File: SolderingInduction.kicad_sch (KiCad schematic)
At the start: 56 parts, among them J1 MC-307, J3 RBP_GPIO_CONN, SW1 SW_Push, SW2 SW_Push, SW3 SW_Push, SW4 SW_Push, SW5 SW_Push, SW6 SW_Push, SW7 SW_Push, SW8 SW_Push, U1 SPX2920M3-3.3_SOT223, U2 CAT24C256, U3 W25Q32JVZP, U4 RP2040, Y1 X322512MMB4SI

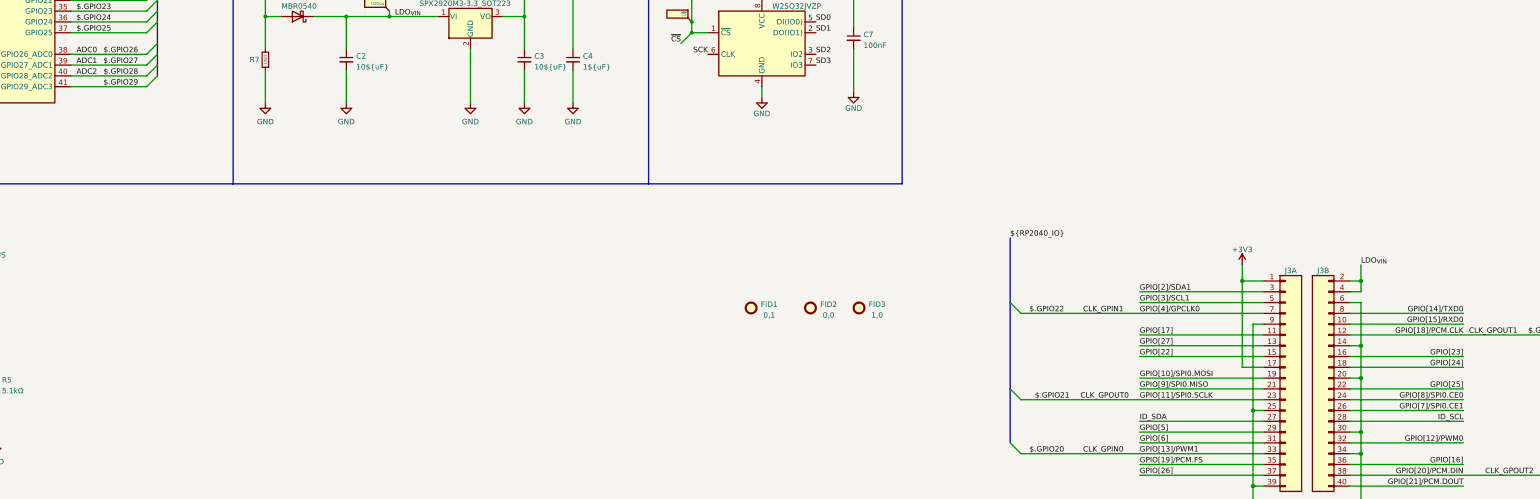
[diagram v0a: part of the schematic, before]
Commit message: Rough layout run to pinheader
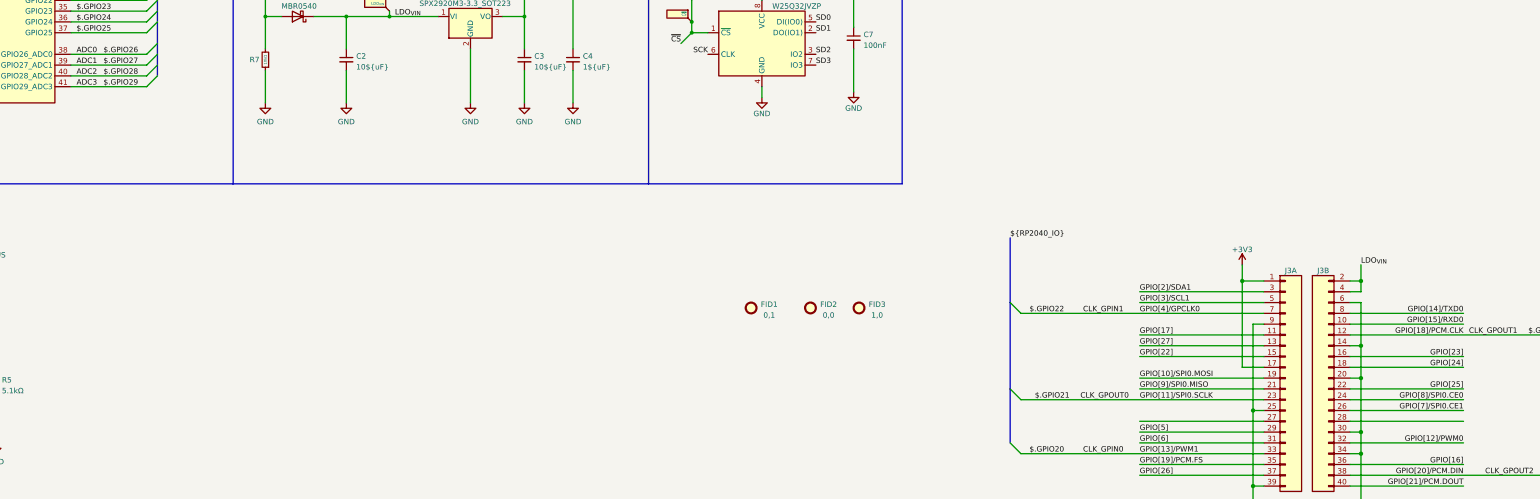
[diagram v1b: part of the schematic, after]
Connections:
- net ID_SCL: no longer J3.28 (Pin_28)
- net ID_SDA: no longer J3.27 (Pin_27)
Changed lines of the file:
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@@
     (effects (font (size 1.27 1.27)) (justify right bottom))
   )
-  (label "BUTTON_DOWN" (at 519.43 49.53 0)
+  (label "ADC3" (at 99.06 104.14 0)
     (effects (font (size 1.27 1.27)) (justify left bottom))
   )
-  (label "ID_SDA" (at 349.25 182.88 0)
+  (label "BUTTON_DOWN" (at 519.43 49.53 0)
     (effects (font (size 1.27 1.27)) (justify left bottom))
   )
@@
     (effects (font (size 1.27 1.27)) (justify left bottom))
   )
-  (label "ID_SCL" (at 425.45 182.88 180)
-    (effects (font (size 1.27 1.27)) (justify right bottom))
-  )
   (label "$.GPIO29" (at 532.13 224.79 0)

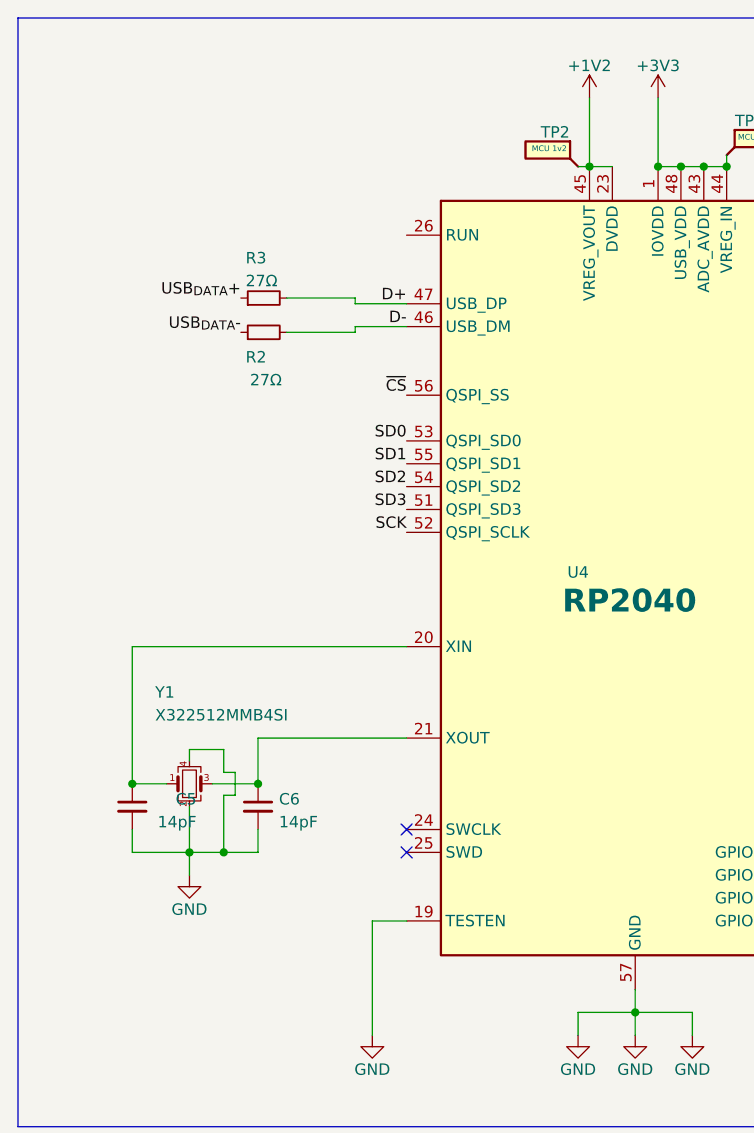
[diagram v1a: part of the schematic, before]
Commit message: SWD pad breakout
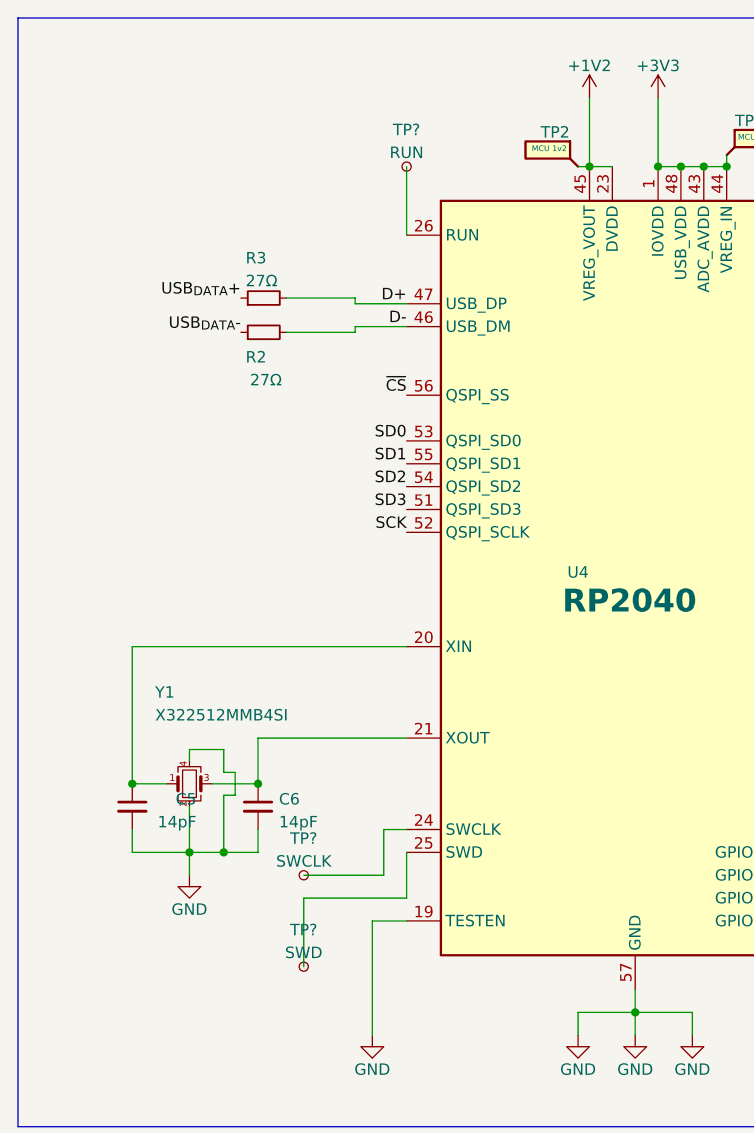
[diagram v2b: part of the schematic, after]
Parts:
- added TP?: SWD, 0:Testpoint_Custom, symbol 4ms_Connector:TestPoint_Small
- added TP?: RUN, 0:Testpoint_Custom, symbol 4ms_Connector:TestPoint_Small
- added TP?: SWCLK, 0:Testpoint_Custom, symbol 4ms_Connector:TestPoint_Small
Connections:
- net at U4.24 (SWCLK): now also TP?.1
- net at U4.25 (SWD): now also TP?.1
- net at U4.26 (RUN): now also TP?.1
- no-connect marks 9 -> 7
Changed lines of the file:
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@@
   (junction (at 431.8 299.72) (diameter 1.016) (color 0 0 0 0)
   )
-  (no_connect (at 46.99 93.98))
-  (no_connect (at 46.99 96.52))
   (no_connect (at 408.94 302.26))
   (no_connect (at 21.59 187.96))
@@
     (stroke (width 0) (type solid) (color 0 0 0 0))
   )
+  (wire (pts (xy 35.56 101.6) (xy 46.99 101.6))
+    (stroke (width 0) (type default) (color 0 0 0 0))
+  )
   (wire (pts (xy 524.51 148.59) (xy 542.29 148.59))
     (stroke (width 0) (type default) (color 0 0 0 0))
@@
     (stroke (width 0) (type solid) (color 0 0 0 0))
   )
+  (wire (pts (xy 44.45 93.98) (xy 46.99 93.98))
+    (stroke (width 0) (type default) (color 0 0 0 0))
+  )
   (bus (pts (xy 118.11 43.18) (xy 118.11 45.72))
     (stroke (width 0) (type default) (color 0 0 0 0))
@@
     (stroke (width 0) (type default) (color 0 0 0 0))
   )
+  (wire (pts (xy 44.45 99.06) (xy 44.45 93.98))
+    (stroke (width 0) (type default) (color 0 0 0 0))
+  )
   (wire (pts (xy 97.79 55.88) (xy 115.57 55.88))
     (stroke (width 0) (type default) (color 0 0 0 0))
@@
     (stroke (width 0) (type default) (color 0 0 0 0))
   )
+  (wire (pts (xy 35.56 99.06) (xy 44.45 99.06))
+    (stroke (width 0) (type default) (color 0 0 0 0))
+  )
   (wire (pts (xy 419.1 309.88) (xy 419.1 312.42))
     (stroke (width 0) (type solid) (color 0 0 0 0))
@@
     (stroke (width 0) (type default) (color 0 0 0 0))
   )
+  (wire (pts (xy 46.99 20.32) (xy 46.99 27.94))
+    (stroke (width 0) (type default) (color 0 0 0 0))
+  )
   (wire (pts (xy 524.51 171.45) (xy 542.29 171.45))
     (stroke (width 0) (type default) (color 0 0 0 0))
@@
     (stroke (width 0) (type default) (color 0 0 0 0))
   )
+  (wire (pts (xy 46.99 101.6) (xy 46.99 96.52))
+    (stroke (width 0) (type default) (color 0 0 0 0))
+  )
   (wire (pts (xy 16.51 96.52) (xy 22.86 96.52))
     (stroke (width 0) (type default) (color 0 0 0 0))
@@
     (stroke (width 0) (type solid) (color 0 0 0 0))
   )
+  (wire (pts (xy 35.56 109.22) (xy 35.56 101.6))
+    (stroke (width 0) (type default) (color 0 0 0 0))
+  )
   (wire (pts (xy 143.51 67.31) (xy 143.51 78.74))
     (stroke (width 0) (type default) (color 0 0 0 0))
@@
     (pin "1")
   )
+  (symbol (lib_id "4ms_Connector:TestPoint_Small") (at 35.56 109.22 90) (unit 1)
+    (in_bom yes) (on_board yes) (fields_autoplaced)
+    (property "Reference" "TP?" (id 0) (at 35.56 105.1392 90))
+    (property "Value" "SWD" (id 1) (at 35.56 107.6761 90))
+    (property "Footprint" "0:Testpoint_Custom" (id 2) (at 35.56 104.14 0)
+      (effects (font (size 1.27 1.27)) hide)
+    )
+    (property "Datasheet" "~" (id 3) (at 35.56 104.14 0)
+      (effects (font (size 1.27 1.27)) hide)
+    )
+    (pin "1")
+  )
   (symbol (lib_id "power:+1V2") (at 143.51 12.7 0) (unit 1)
     (in_bom yes) (on_board yes) (fields_autoplaced)
@@
     (pin "8")
   )
+  (symbol (lib_id "4ms_Connector:TestPoint_Small") (at 46.99 20.32 90) (unit 1)
+    (in_bom yes) (on_board yes) (fields_autoplaced)
+    (property "Reference" "TP?" (id 0) (at 46.99 16.2392 90))
+    (property "Value" "RUN" (id 1) (at 46.99 18.7761 90))
+    (property "Footprint" "0:Testpoint_Custom" (id 2) (at 46.99 15.24 0)
+      (effects (font (size 1.27 1.27)) hide)
+    )
+    (property "Datasheet" "~" (id 3) (at 46.99 15.24 0)
+      (effects (font (size 1.27 1.27)) hide)
+    )
+    (pin "1")
+  )
   (symbol (lib_id "power:+3V3") (at 373.38 146.05 0) (unit 1)
     (in_bom yes) (on_board yes) (fields_autoplaced)
@@
     (pin "1")
   )
+  (symbol (lib_id "4ms_Connector:TestPoint_Small") (at 35.56 99.06 90) (unit 1)
+    (in_bom yes) (on_board yes) (fields_autoplaced)
+    (property "Reference" "TP?" (id 0) (at 35.56 94.9792 90))
+    (property "Value" "SWCLK" (id 1) (at 35.56 97.5161 90))
+    (property "Footprint" "0:Testpoint_Custom" (id 2) (at 35.56 93.98 0)
+      (effects (font (size 1.27 1.27)) hide)
+    )
+    (property "Datasheet" "~" (id 3) (at 35.56 93.98 0)
+      (effects (font (size 1.27 1.27)) hide)
+    )
+    (pin "1")
+  )
   (symbol (lib_id "power:+1V2") (at 67.31 12.7 0) (unit 1)
     (in_bom yes) (on_board yes) (fields_autoplaced)
@@
       (reference "TP12") (unit 1) (value "~{CS}") (footprint "0:Testpoint_Custom")
     )
+    (path "/a7e70440-f347-43ab-bb7e-527f8e18d4e1"
+      (reference "TP?") (unit 1) (value "SWD") (footprint "0:Testpoint_Custom")
+    )
+    (path "/b127f413-4a75-4fc1-94fb-a31ea2a5f1e7"
+      (reference "TP?") (unit 1) (value "RUN") (footprint "0:Testpoint_Custom")
+    )
+    (path "/b156a65f-8828-4aba-9f95-310a095027c2"
+      (reference "TP?") (unit 1) (value "SWCLK") (footprint "0:Testpoint_Custom")
+    )
     (path "/466f2e5a-a0ef-47a2-ba92-b7fc850cdf6c"

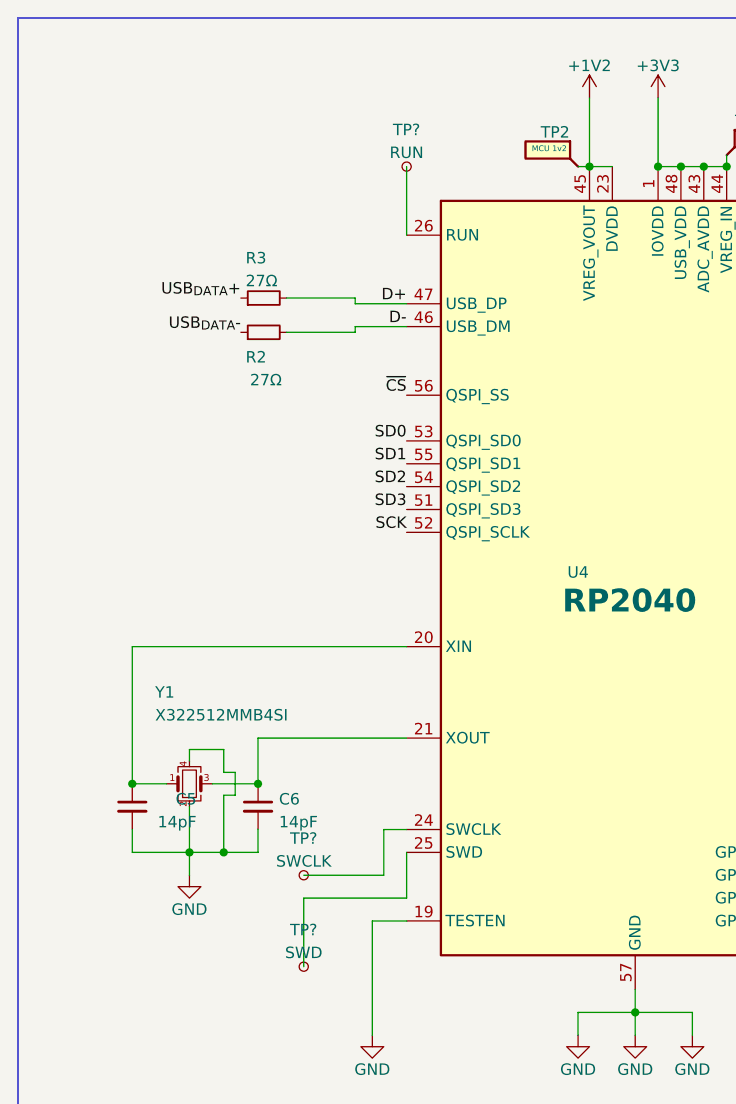
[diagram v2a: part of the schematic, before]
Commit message: Fiducials, Testpoints, routing cleanup
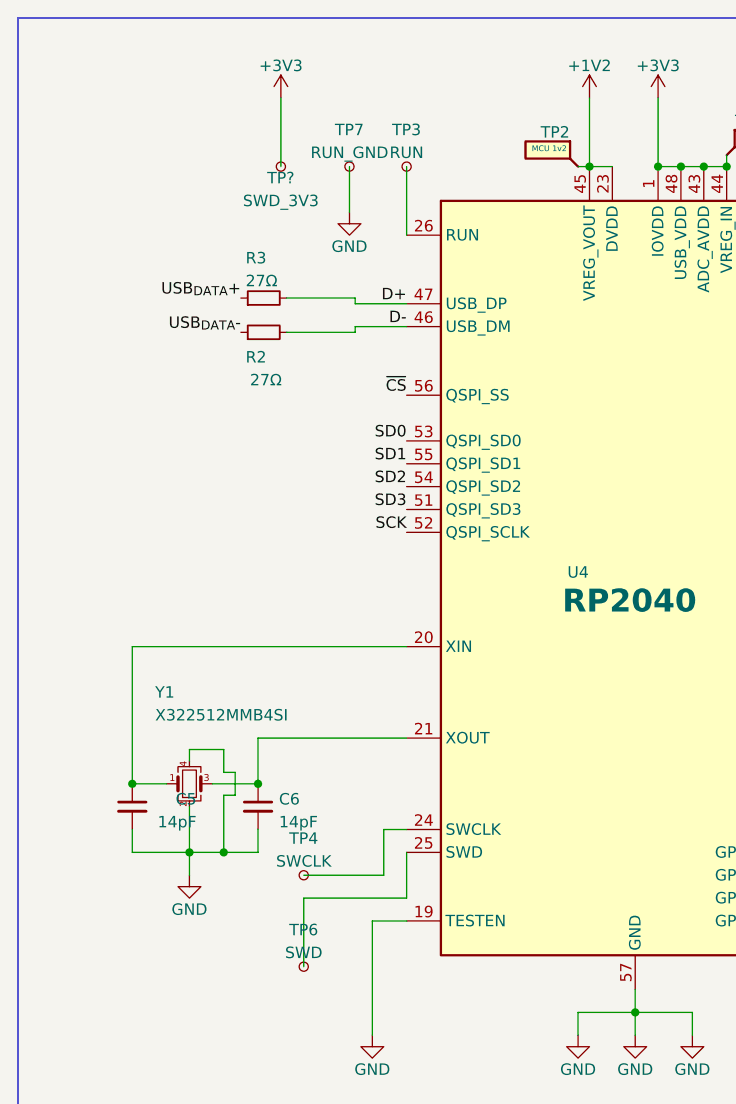
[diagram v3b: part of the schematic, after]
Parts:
- added TP7: RUN_GND, 0:Testpoint_Custom, symbol 4ms_Connector:TestPoint_Small
- added TP?: SWD_3V3, 0:Testpoint_Custom, symbol 4ms_Connector:TestPoint_Small
- gave numbers to parts that had none: 3
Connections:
- net +3V3: now also TP?.1
- net GND: now also TP7.1
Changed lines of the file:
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@@
     (stroke (width 0) (type default) (color 0 0 0 0))
   )
+  (wire (pts (xy 40.64 20.32) (xy 40.64 25.4))
+    (stroke (width 0) (type default) (color 0 0 0 0))
+  )
   (bus (pts (xy 118.11 99.06) (xy 118.11 101.6))
     (stroke (width 0) (type default) (color 0 0 0 0))
@@
     (stroke (width 0) (type default) (color 0 0 0 0))
   )
+  (wire (pts (xy 33.02 12.7) (xy 33.02 20.32))
+    (stroke (width 0) (type default) (color 0 0 0 0))
+  )
   (wire (pts (xy 220.98 36.83) (xy 220.98 38.1))
     (stroke (width 0) (type default) (color 0 0 0 0))
@@
     )
   )
+  (symbol (lib_id "power:+3V3") (at 33.02 12.7 0) (unit 1)
+    (in_bom yes) (on_board yes) (fields_autoplaced)
+    (property "Reference" "#PWR?" (id 0) (at 33.02 16.51 0)
+      (effects (font (size 1.27 1.27)) hide)
+    )
+    (property "Value" "+3V3" (id 1) (at 33.02 9.1242 0))
+    (property "Footprint" "" (id 2) (at 33.02 12.7 0)
+      (effects (font (size 1.27 1.27)) hide)
+    )
+    (property "Datasheet" "" (id 3) (at 33.02 12.7 0)
+      (effects (font (size 1.27 1.27)) hide)
+    )
+    (pin "1")
+  )
+  (symbol (lib_id "4ms_Connector:TestPoint_Small") (at 33.02 20.32 90) (unit 1)
+    (in_bom yes) (on_board yes)
+    (property "Reference" "TP?" (id 0) (at 33.02 21.59 90))
+    (property "Value" "SWD_3V3" (id 1) (at 33.02 24.13 90))
+    (property "Footprint" "0:Testpoint_Custom" (id 2) (at 33.02 15.24 0)
+      (effects (font (size 1.27 1.27)) hide)
+    )
+    (property "Datasheet" "~" (id 3) (at 33.02 15.24 0)
+      (effects (font (size 1.27 1.27)) hide)
+    )
+    (pin "1")
+  )
   (symbol (lib_id "Switch:SW_Push") (at 514.35 38.1 0) (unit 1)
     (in_bom yes) (on_board yes) (fields_autoplaced)
@@
     (pin "1")
   )
+  (symbol (lib_id "4ms_Connector:TestPoint_Small") (at 40.64 20.32 90) (unit 1)
+    (in_bom yes) (on_board yes) (fields_autoplaced)
+    (property "Reference" "TP7" (id 0) (at 40.64 16.2392 90))
+    (property "Value" "RUN_GND" (id 1) (at 40.64 18.7761 90))
+    (property "Footprint" "0:Testpoint_Custom" (id 2) (at 40.64 15.24 0)
+      (effects (font (size 1.27 1.27)) hide)
+    )
+    (property "Datasheet" "~" (id 3) (at 40.64 15.24 0)
+      (effects (font (size 1.27 1.27)) hide)
+    )
+    (pin "1")
+  )
   (symbol (lib_id "power:VBUS") (at 80.01 147.32 0) (unit 1)
     (in_bom yes) (on_board yes) (fields_autoplaced)
@@
   (symbol (lib_id "4ms_Connector:TestPoint_Small") (at 35.56 109.22 90) (unit 1)
     (in_bom yes) (on_board yes) (fields_autoplaced)
-    (property "Reference" "TP?" (id 0) (at 35.56 105.1392 90))
+    (property "Reference" "TP6" (id 0) (at 35.56 105.1392 90))
     (property "Value" "SWD" (id 1) (at 35.56 107.6761 90))
     (property "Footprint" "0:Testpoint_Custom" (id 2) (at 35.56 104.14 0)
@@
   (symbol (lib_id "4ms_Connector:TestPoint_Small") (at 46.99 20.32 90) (unit 1)
     (in_bom yes) (on_board yes) (fields_autoplaced)
-    (property "Reference" "TP?" (id 0) (at 46.99 16.2392 90))
+    (property "Reference" "TP3" (id 0) (at 46.99 16.2392 90))
     (property "Value" "RUN" (id 1) (at 46.99 18.7761 90))
     (property "Footprint" "0:Testpoint_Custom" (id 2) (at 46.99 15.24 0)
@@
   (symbol (lib_id "4ms_Connector:TestPoint_Small") (at 35.56 99.06 90) (unit 1)
     (in_bom yes) (on_board yes) (fields_autoplaced)
-    (property "Reference" "TP?" (id 0) (at 35.56 94.9792 90))
+    (property "Reference" "TP4" (id 0) (at 35.56 94.9792 90))
     (property "Value" "SWCLK" (id 1) (at 35.56 97.5161 90))
     (property "Footprint" "0:Testpoint_Custom" (id 2) (at 35.56 93.98 0)
@@
     (pin "1")
   )
+  (symbol (lib_id "4ms_Power-symbol:GND") (at 40.64 25.4 0) (unit 1)
+    (in_bom yes) (on_board yes)
+    (property "Reference" "#PWR0114" (id 0) (at 40.64 31.75 0)
+      (effects (font (size 1.27 1.27)) hide)
+    )
+    (property "Value" "GND" (id 1) (at 40.64 29.21 0))
+    (property "Footprint" "" (id 2) (at 40.64 25.4 0)
+      (effects (font (size 1.27 1.27)) hide)
+    )
+    (property "Datasheet" "" (id 3) (at 40.64 25.4 0)
+      (effects (font (size 1.27 1.27)) hide)
+    )
+    (pin "1")
+  )
   (symbol (lib_id "Device:C_Small") (at 162.56 97.79 0) (unit 1)
     (in_bom yes) (on_board yes)
@@
       (reference "#PWR0113") (unit 1) (value "GND") (footprint "")
     )
+    (path "/fc1fe0f7-0d31-45b9-a3c0-6f0bd86ebdeb"
+      (reference "#PWR0114") (unit 1) (value "GND") (footprint "")
+    )
     (path "/bcb4d045-95f6-4270-90fb-aaa97f3b5edc"
       (reference "#PWR0117") (unit 1) (value "GND") (footprint "")
@@
       (reference "#PWR0160") (unit 1) (value "+3V3") (footprint "")
     )
+    (path "/5e3b4ed3-8852-4e75-9256-14b7f32ff647"
+      (reference "#PWR?") (unit 1) (value "+3V3") (footprint "")
+    )
     (path "/7d0a9912-f067-470e-a556-0ab8e7970517"
       (reference "C1") (unit 1) (value "1μF") (footprint "Capacitor_SMD:C_0805_2012Metric")
@@
       (reference "TP2") (unit 1) (value "MCU 1v2") (footprint "0:Testpoint_Custom")
     )
+    (path "/b127f413-4a75-4fc1-94fb-a31ea2a5f1e7"
+      (reference "TP3") (unit 1) (value "RUN") (footprint "0:Testpoint_Custom")
+    )
+    (path "/b156a65f-8828-4aba-9f95-310a095027c2"
+      (reference "TP4") (unit 1) (value "SWCLK") (footprint "0:Testpoint_Custom")
+    )
     (path "/291a849f-2383-40ad-9f6c-802f889def5d"
       (reference "TP5") (unit 1) (value "LED DATA") (footprint "0:Testpoint_Custom")
     )
+    (path "/a7e70440-f347-43ab-bb7e-527f8e18d4e1"
+      (reference "TP6") (unit 1) (value "SWD") (footprint "0:Testpoint_Custom")
+    )
+    (path "/88c7d4d8-b1fc-4940-8e8a-0327497ff94d"
+      (reference "TP7") (unit 1) (value "RUN_GND") (footprint "0:Testpoint_Custom")
+    )
     (path "/e15e5ff1-7166-4d69-94e7-6880a8a66b9c"
       (reference "TP8") (unit 1) (value "VBUS") (footprint "0:Testpoint_Custom")
@@
       (reference "TP12") (unit 1) (value "~{CS}") (footprint "0:Testpoint_Custom")
     )
-    (path "/a7e70440-f347-43ab-bb7e-527f8e18d4e1"
-      (reference "TP?") (unit 1) (value "SWD") (footprint "0:Testpoint_Custom")
-    )
-    (path "/b127f413-4a75-4fc1-94fb-a31ea2a5f1e7"
-      (reference "TP?") (unit 1) (value "RUN") (footprint "0:Testpoint_Custom")
-    )
-    (path "/b156a65f-8828-4aba-9f95-310a095027c2"
-      (reference "TP?") (unit 1) (value "SWCLK") (footprint "0:Testpoint_Custom")
+    (path "/62b7d856-4b8d-422d-8f25-7b7b19efeb20"
+      (reference "TP?") (unit 1) (value "SWD_3V3") (footprint "0:Testpoint_Custom")
     )
     (path "/466f2e5a-a0ef-47a2-ba92-b7fc850cdf6c"
